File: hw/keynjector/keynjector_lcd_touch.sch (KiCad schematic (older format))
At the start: 7 parts, among them J3 FH12A-40S-0.5SH(55), U4 ADS7843

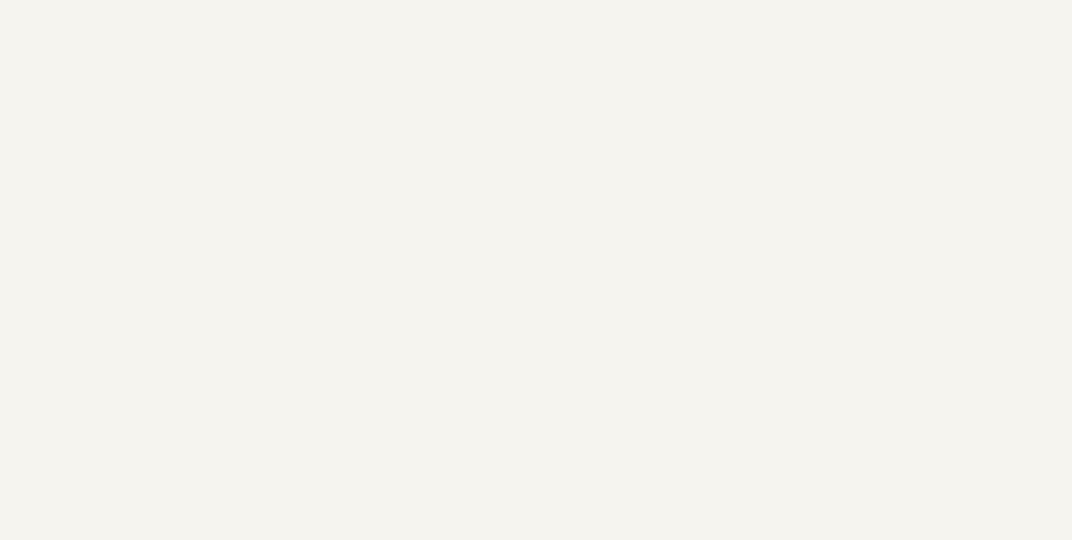
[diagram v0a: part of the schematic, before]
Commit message: added license text to KiCad sheets
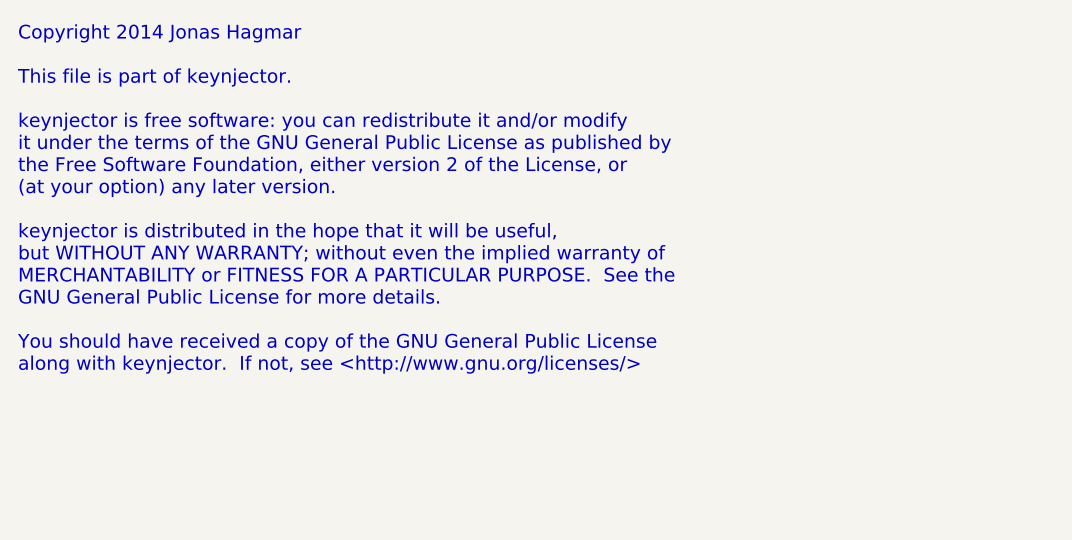
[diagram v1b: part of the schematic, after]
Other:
- note added: "Copyright 2014 Jonas Hagmar\n\nThis file is part of keynjector.\n\nkeynjector is free software: you can redistribute it and/or modify\nit under the terms of the GNU General Public License as published by\nthe Free Software Foundation, either version 2 of the License, or\n(at your option) any later version.\n\nkeynjector is distributed in the hope that it will be useful,\nbut WITHOUT ANY WARRANTY;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"
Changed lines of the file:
@@
 Sheet 6 7
 Title ""
-Date "6 nov 2014"
+Date "2 dec 2014"
 Rev ""
 Comp ""
@@
 	1    0    0    -1
 $EndComp
+Text Notes 900  850  0    60   ~ 0
+Copyright 2014 Jonas Hagmar\n\nThis file is part of keynjector.\n\nkeynjector is free software: you can redistribute it and/or modify\nit under the terms of the GNU General Public License as published by\nthe Free Software Foundation, either version 2 of the License, or\n(at your option) any later version.\n\nkeynjector is distributed in the hope that it will be useful,\nbut WITHOUT ANY WARRANTY; without even the implied warranty of\nMERCHANTABILITY or FITNESS FOR A PARTICULAR PURPOSE.  See the\nGNU General Public License for more details.\n\nYou should have received a copy of the GNU General Public License\nalong with keynjector.  If not, see <http://www.gnu.org/licenses/>
 $EndSCHEMATC
